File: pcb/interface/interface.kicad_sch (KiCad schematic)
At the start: 15 parts, among them J1 SEGMENTS, J16 BUS_IN, J17 BUS_OUT, J5 SELECT, Q1 MMBT3904, Q2 MMBT3904, Q3 MMBT3904, Q4 MMBT3904, U1 74HC595, U2 74HC595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

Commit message: cleaned up, reworked and (so far) finalized the interface board
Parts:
- U1, U2, U3: footprint Package_SO:SO-16_3.9x9.9mm_P1.27mm -> Package_SO:SOIC-16_3.9x9.9mm_P1.27mm
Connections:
- net DBD_DP is gone; now on net DP: U1.5 (QF)
- net DBD_DISPLAY1_GND renamed DISPLAY1_GND
- net DBD_DISPLAY2_GND renamed DISPLAY2_GND
- net DBD_DISPLAY3_GND renamed DISPLAY3_GND
- net DBD_DISPLAY4_GND renamed DISPLAY4_GND
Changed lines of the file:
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@@
     )
   )
-  (global_label "DBD_DISPLAY3_GND" (shape input) (at 57.15 173.99 180) (fields_autoplaced)
-    (effects (font (size 1.27 1.27)) (justify right))
-    (property "Intersheetrefs" "${INTERSHEET_REFS}" (at 35.78 173.99 0)
+  (global_label "DISPLAY3_GND" (shape input) (at 57.15 173.99 180) (fields_autoplaced)
+    (effects (font (size 1.27 1.27)) (justify right))
+    (property "Intersheetrefs" "${INTERSHEET_REFS}" (at 40.5576 173.99 0)
       (effects (font (size 1.27 1.27)) (justify right) hide)
     )
@@
     )
   )
-  (global_label "DBD_DP" (shape input) (at 219.71 77.47 0) (fields_autoplaced)
-    (effects (font (size 1.27 1.27)) (justify left))
-    (property "Intersheetrefs" "${INTERSHEET_REFS}" (at 230.0128 77.47 0)
+  (global_label "DP" (shape input) (at 219.71 77.47 0) (fields_autoplaced)
+    (effects (font (size 1.27 1.27)) (justify left))
+    (property "Intersheetrefs" "${INTERSHEET_REFS}" (at 225.2352 77.47 0)
       (effects (font (size 1.27 1.27)) (justify left) hide)
     )
@@
     )
   )
-  (global_label "DBD_DISPLAY2_GND" (shape input) (at 57.15 176.53 180) (fields_autoplaced)
-    (effects (font (size 1.27 1.27)) (justify right))
-    (property "Intersheetrefs" "${INTERSHEET_REFS}" (at 35.78 176.53 0)
+  (global_label "DISPLAY2_GND" (shape input) (at 57.15 176.53 180) (fields_autoplaced)
+    (effects (font (size 1.27 1.27)) (justify right))
+    (property "Intersheetrefs" "${INTERSHEET_REFS}" (at 40.5576 176.53 0)
       (effects (font (size 1.27 1.27)) (justify right) hide)
     )
@@
     )
   )
-  (global_label "DBD_DISPLAY4_GND" (shape input) (at 57.15 171.45 180) (fields_autoplaced)
-    (effects (font (size 1.27 1.27)) (justify right))
-    (property "Intersheetrefs" "${INTERSHEET_REFS}" (at 35.78 171.45 0)
-      (effects (font (size 1.27 1.27)) (justify right) hide)
-    )
-  )
-  (global_label "DBD_DISPLAY1_GND" (shape input) (at 243.84 55.88 0) (fields_autoplaced)
-    (effects (font (size 1.27 1.27)) (justify left))
-    (property "Intersheetrefs" "${INTERSHEET_REFS}" (at 265.21 55.88 0)
+  (global_label "DISPLAY4_GND" (shape input) (at 57.15 171.45 180) (fields_autoplaced)
+    (effects (font (size 1.27 1.27)) (justify right))
+    (property "Intersheetrefs" "${INTERSHEET_REFS}" (at 40.5576 171.45 0)
+      (effects (font (size 1.27 1.27)) (justify right) hide)
+    )
+  )
+  (global_label "DISPLAY1_GND" (shape input) (at 243.84 55.88 0) (fields_autoplaced)
+    (effects (font (size 1.27 1.27)) (justify left))
+    (property "Intersheetrefs" "${INTERSHEET_REFS}" (at 260.4324 55.88 0)
       (effects (font (size 1.27 1.27)) (justify left) hide)
     )
@@
     )
   )
-  (global_label "DBD_DISPLAY4_GND" (shape input) (at 243.84 132.08 0) (fields_autoplaced)
-    (effects (font (size 1.27 1.27)) (justify left))
-    (property "Intersheetrefs" "${INTERSHEET_REFS}" (at 265.21 132.08 0)
+  (global_label "DISPLAY4_GND" (shape input) (at 243.84 132.08 0) (fields_autoplaced)
+    (effects (font (size 1.27 1.27)) (justify left))
+    (property "Intersheetrefs" "${INTERSHEET_REFS}" (at 260.4324 132.08 0)
       (effects (font (size 1.27 1.27)) (justify left) hide)
     )
@@
     )
   )
-  (global_label "DBD_DISPLAY2_GND" (shape input) (at 243.84 81.28 0) (fields_autoplaced)
-    (effects (font (size 1.27 1.27)) (justify left))
-    (property "Intersheetrefs" "${INTERSHEET_REFS}" (at 265.21 81.28 0)
+  (global_label "DISPLAY2_GND" (shape input) (at 243.84 81.28 0) (fields_autoplaced)
+    (effects (font (size 1.27 1.27)) (justify left))
+    (property "Intersheetrefs" "${INTERSHEET_REFS}" (at 260.4324 81.28 0)
       (effects (font (size 1.27 1.27)) (justify left) hide)
     )
@@
     )
   )
-  (global_label "DBD_DISPLAY3_GND" (shape input) (at 243.84 106.68 0) (fields_autoplaced)
-    (effects (font (size 1.27 1.27)) (justify left))
-    (property "Intersheetrefs" "${INTERSHEET_REFS}" (at 265.21 106.68 0)
-      (effects (font (size 1.27 1.27)) (justify left) hide)
-    )
-  )
-  (global_label "DBD_DISPLAY1_GND" (shape input) (at 57.15 179.07 180) (fields_autoplaced)
-    (effects (font (size 1.27 1.27)) (justify right))
-    (property "Intersheetrefs" "${INTERSHEET_REFS}" (at 35.78 179.07 0)
+  (global_label "DISPLAY3_GND" (shape input) (at 243.84 106.68 0) (fields_autoplaced)
+    (effects (font (size 1.27 1.27)) (justify left))
+    (property "Intersheetrefs" "${INTERSHEET_REFS}" (at 260.4324 106.68 0)
+      (effects (font (size 1.27 1.27)) (justify left) hide)
+    )
+  )
+  (global_label "DISPLAY1_GND" (shape input) (at 57.15 179.07 180) (fields_autoplaced)
+    (effects (font (size 1.27 1.27)) (justify right))
+    (property "Intersheetrefs" "${INTERSHEET_REFS}" (at 40.5576 179.07 0)
       (effects (font (size 1.27 1.27)) (justify right) hide)
     )
@@
       (effects (font (size 1.27 1.27)) (justify left))
     )
-    (property "Footprint" "Package_SO:SO-16_3.9x9.9mm_P1.27mm" (at 194.31 74.93 0)
+    (property "Footprint" "Package_SO:SOIC-16_3.9x9.9mm_P1.27mm" (at 194.31 74.93 0)
       (effects (font (size 1.27 1.27)) hide)
     )
@@
       (effects (font (size 1.27 1.27)) (justify left))
     )
-    (property "Footprint" "Package_SO:SO-16_3.9x9.9mm_P1.27mm" (at 153.67 74.93 0)
+    (property "Footprint" "Package_SO:SOIC-16_3.9x9.9mm_P1.27mm" (at 153.67 74.93 0)
       (effects (font (size 1.27 1.27)) hide)
     )
@@
       (effects (font (size 1.27 1.27)) (justify left))
     )
-    (property "Footprint" "Package_SO:SO-16_3.9x9.9mm_P1.27mm" (at 111.76 74.93 0)
-      (effects (font (size 1.27 1.27)) hide)
-    )
+    (property "Footprint" "Package_SO:SOIC-16_3.9x9.9mm_P1.27mm" (at 111.76 74.93 0)
+      (effects (font (size 1.27 1.27)) hide)
+    )

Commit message: added missing resistors to the interface board
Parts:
- added R1, R10, R11, R12, R13, R14, R15, R16, R17, R2, R3, R4, R5, R6, R7, R8, R9: 220R, Resistor_SMD:R_0603_1608Metric, symbol Device:R
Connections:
- net A: now also R10.2; no longer U3.1 (QB)
- net B: now also R9.2; no longer U3.15 (QA)
- net C: now also R13.2; no longer U3.4 (QE)
- net D: now also R4.2; no longer U2.3 (QD)
- net DP: now also R17.2; no longer U1.5 (QF)
- net E: now also R6.2; no longer U2.5 (QF)
- net F: now also R8.2; no longer U2.7 (QH)
- net G: now also R7.2; no longer U2.6 (QG)
- net H: now also R16.2; no longer U3.7 (QH)
- net I: now also R14.2; no longer U3.5 (QF)
- net J: now also R12.2; no longer U3.3 (QD)
- net K: now also R11.2; no longer U3.2 (QC)
- net L: now also R15.2; no longer U3.6 (QG)
- net M: now also R1.2; no longer U2.15 (QA)
- net N: now also R3.2; no longer U2.2 (QC)
- net O: now also R5.2; no longer U2.4 (QE)
- net P: now also R2.2; no longer U2.1 (QB)
- new net: R5.1, U2.4 (QE)
- new net: R16.1, U3.7 (QH)
- new net: R2.1, U2.1 (QB)
- new net: R17.1, U1.5 (QF)
- new net: R7.1, U2.6 (QG)
- new net: R1.1, U2.15 (QA)
- new net: R15.1, U3.6 (QG)
- new net: R6.1, U2.5 (QF)
- new net: R13.1, U3.4 (QE)
- new net: R8.1, U2.7 (QH)
- new net: R14.1, U3.5 (QF)
- new net: R10.1, U3.1 (QB)
- new net: R3.1, U2.2 (QC)
- new net: R11.1, U3.2 (QC)
- new net: R12.1, U3.3 (QD)
- new net: R9.1, U3.15 (QA)
- new net: R4.1, U2.3 (QD)

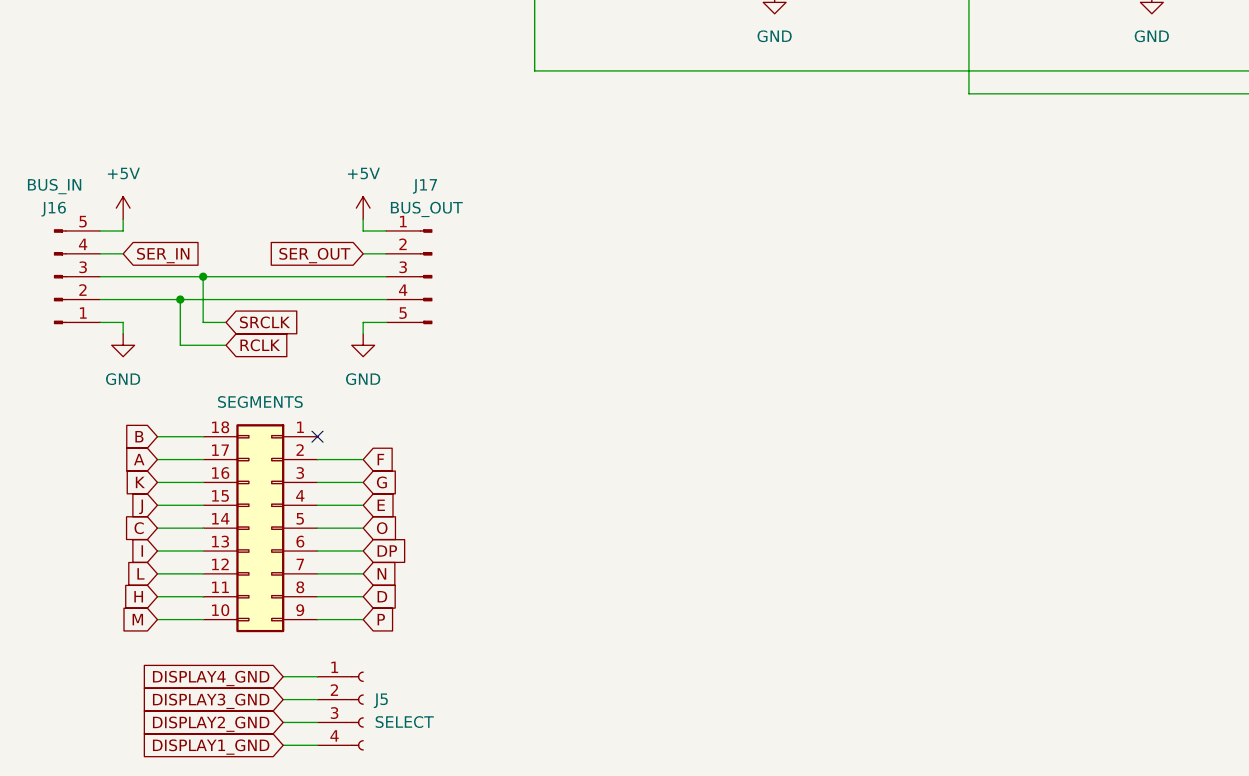
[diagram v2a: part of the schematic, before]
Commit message: added missing input pulldown resistors to the interface board
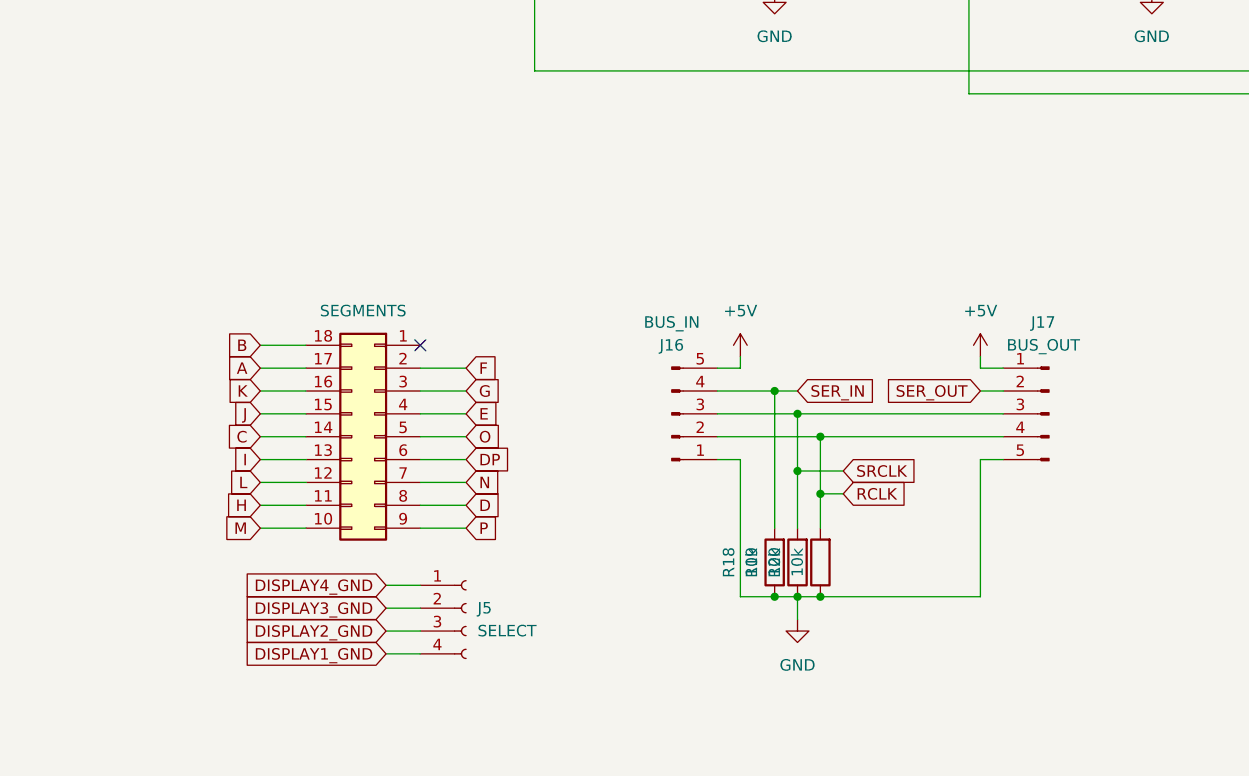
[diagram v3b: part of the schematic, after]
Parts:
- added R18, R19, R20: 10k, Resistor_SMD:R_0603_1608Metric, symbol Device:R
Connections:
- net GND: now also R18.1, R19.1, R20.1
- net RCLK: now also R20.2
- net SER_IN: now also R18.2
- net SRCLK: now also R19.2
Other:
- moved on the sheet: J16, J17, J5
